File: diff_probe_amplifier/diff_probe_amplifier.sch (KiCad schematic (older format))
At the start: 81 parts, among them J1 Triax_inner, J2 Triax_outer, J3 Spring+S, J4 Spring+G, J5 Spring-G, J6 Spring-S, J7 IN+, J8 IN-, SW1 GAIN, U1 R1283K001C, U2 OPA659, U3 OPA659, U4 OPA659

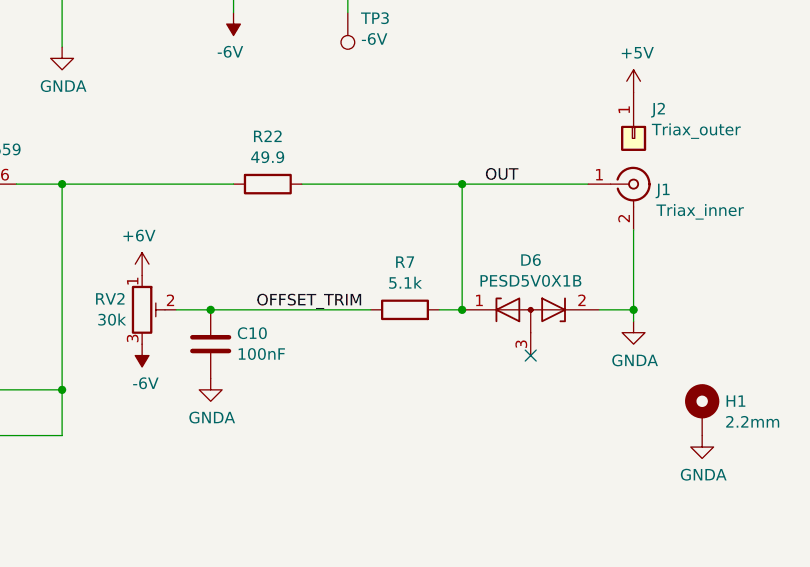
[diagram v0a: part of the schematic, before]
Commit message: Reorganize repository
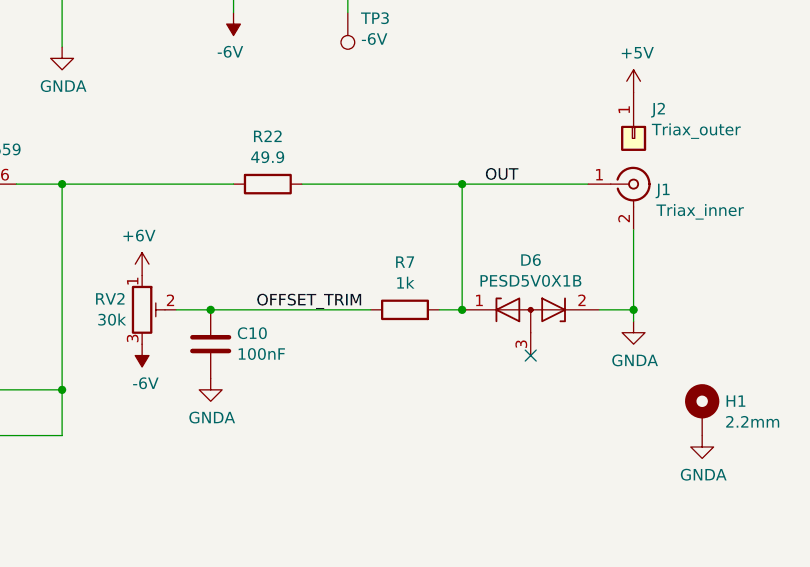
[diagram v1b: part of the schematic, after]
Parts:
- R7: value 5.1k -> 1k
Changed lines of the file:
@@
 P 9550 5650
 F 0 "R7" V 9757 5650 50  0000 C CNN
-F 1 "5.1k" V 9666 5650 50  0000 C CNN
+F 1 "1k" V 9666 5650 50  0000 C CNN
 F 2 "Resistor_SMD:R_0603_1608Metric" V 9480 5650 50  0001 C CNN
 F 3 "~" H 9550 5650 50  0001 C CNN

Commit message: Revision 4
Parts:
- removed C10: 100nF, Capacitor_SMD:C_0603_1608Metric, symbol Device:C
- removed J1: Triax_inner, oscilloscope-probes:COAX_2MM, symbol Connector:Conn_Coaxial
- removed J2: Triax_outer, oscilloscope-probes:TRIAX_OUTER_3MM, symbol Connector_Generic:Conn_01x01
- added J1: Conn_Triaxial, oscilloscope-probes:TRIAX_SOLDER, symbol oscilloscope_probes:Conn_Triaxial
- added TP7: IN+, TestPoint:TestPoint_Pad_D2.5mm, symbol Connector:TestPoint
- added TP8: IN-, TestPoint:TestPoint_Pad_D2.5mm, symbol Connector:TestPoint
- C16, C17: value 8-30pF -> 4.5-20pF; footprint Capacitor_SMD:C_Trimmer_Murata_TZC3 -> oscilloscope-probes:C_Trimmer_Knowles_JZ_JR; Mfg EW -> Knowles; Mfg Part No SGC3S300NM -> JZ200; Notes (none) -> Alternative: JR200
- D1, D2: value NSR05T30 -> SBR1A20; Mfg ON -> Diodes Inc.; Mfg Part No NSR05T30XV2T5G -> SBR1A20
- J7, J8: footprint oscilloscope-probes:RF11-27A-T-00-50-G -> oscilloscope-probes:MMCX_Molex_73415-0961_Horizontal_1.6mm-PCB; Mfg Adam Tech -> Molex; Mfg Part No RF11-27A-T-00-50-G -> 0734150963
- L1, L2, L9: value MMZ1608B601 -> BLM18KG102
- R4: renamed from R?; value N/A -> 22k
- RV1, RV2: value 30k -> 25k; footprint Potentiometer_SMD:Potentiometer_Bourns_TC33X_Vertical -> Potentiometer_SMD:Potentiometer_Bourns_3314J_Vertical; Mfg Part No TC33X-2-303E -> 3314J-1-253E
- SW1: footprint oscilloscope-probes:78HF01GWRT -> oscilloscope-probes:JS202011JCQN; Mfg Grayhill -> C&K; Mfg Part No 78HF01GWRT -> JS202011JCQN
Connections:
- net +5V: now also J1.3
- net +6V: now also RV2.3; no longer R8.2, RV2.1
- net -6V: now also D3.1 (K), RV2.1; no longer RV2.3
- net CONN_IN+: now also TP7.1
- net CONN_IN-: now also TP8.1
- net GNDA: now also R8.2, J1.2 (Ext); no longer D3.1 (K)
- net OUT: now also J1.1 (In)
- net at C11.2, R15.1, R17.1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: no longer R4.2
- net at C1.1, R14.2, R16.1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: no longer R4.1
- net at R17.2, SW1.1 (A): now also R4.2
- net at R16.2, SW1.2 (B): now also R4.1
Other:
- note added: "Probe tips have divider resistor and capacitor near the tip to minimize\ncapacitance.\nThe input impedance is 500 kohm || 6-26 pF.\nInput voltage range is +-3 V."
- note removed: "Probe tips have divider resistor and capacitor near the tip to minimize\ncapacitance. For 10x tweezers this is 9.53 Mohm || 1.2 pF.\nThe input impedance is 500 kohm || 10-30 pF.\nInput voltage range is +-3 V."
- moved on the sheet: R16, R17, R4
